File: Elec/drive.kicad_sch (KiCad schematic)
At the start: 37 parts, among them J1 PSU, J2 Conn_01x40, J3 Comm_Conn1, J4 Comm_Conn2, U1 DRV8434SPWPR, U2 DRV8434SPWPR

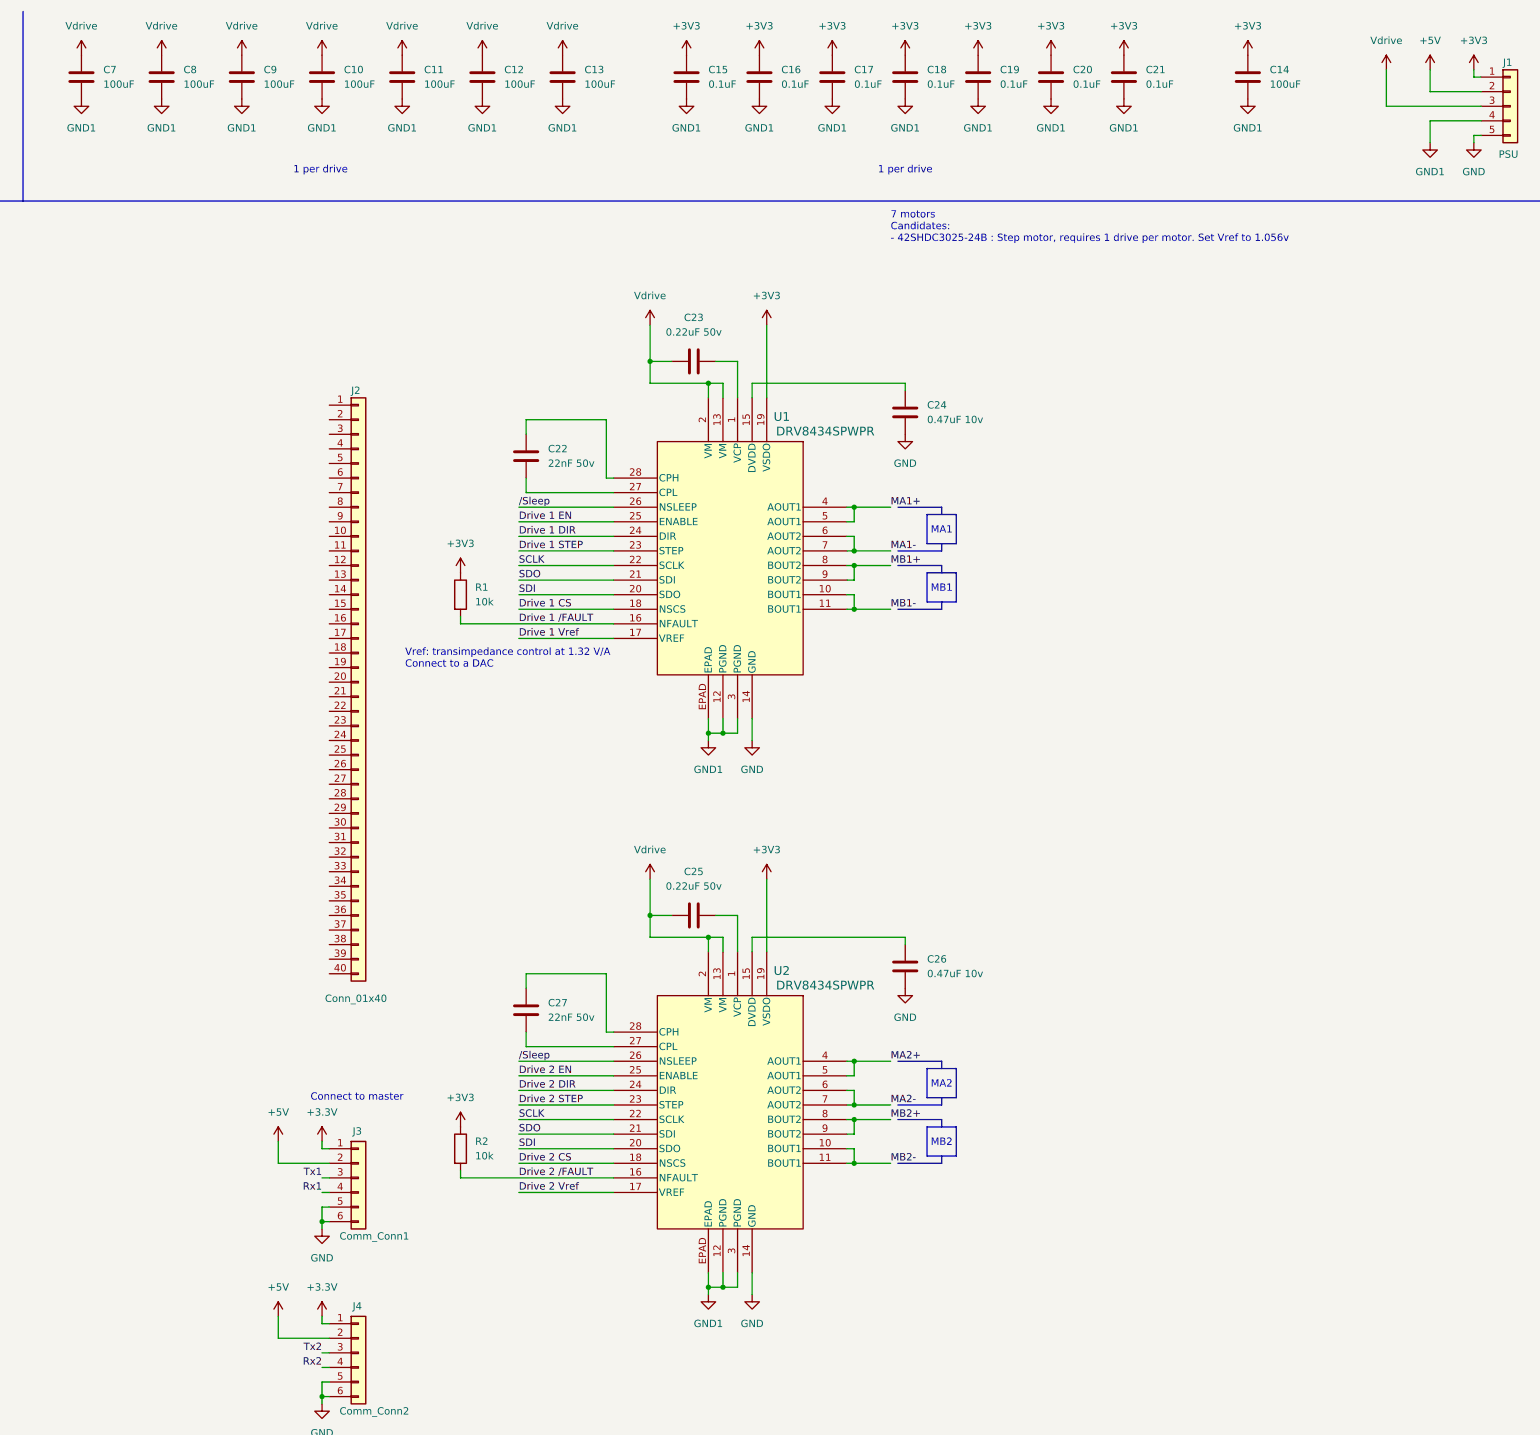
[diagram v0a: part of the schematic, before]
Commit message: Starting integration of the DRV8313PWPR drive
This drive supports BLDCs and BDCs.
Link: https://www.digikey.ca/en/products/detail/texas-instruments/DRV8313PWPR/3775439
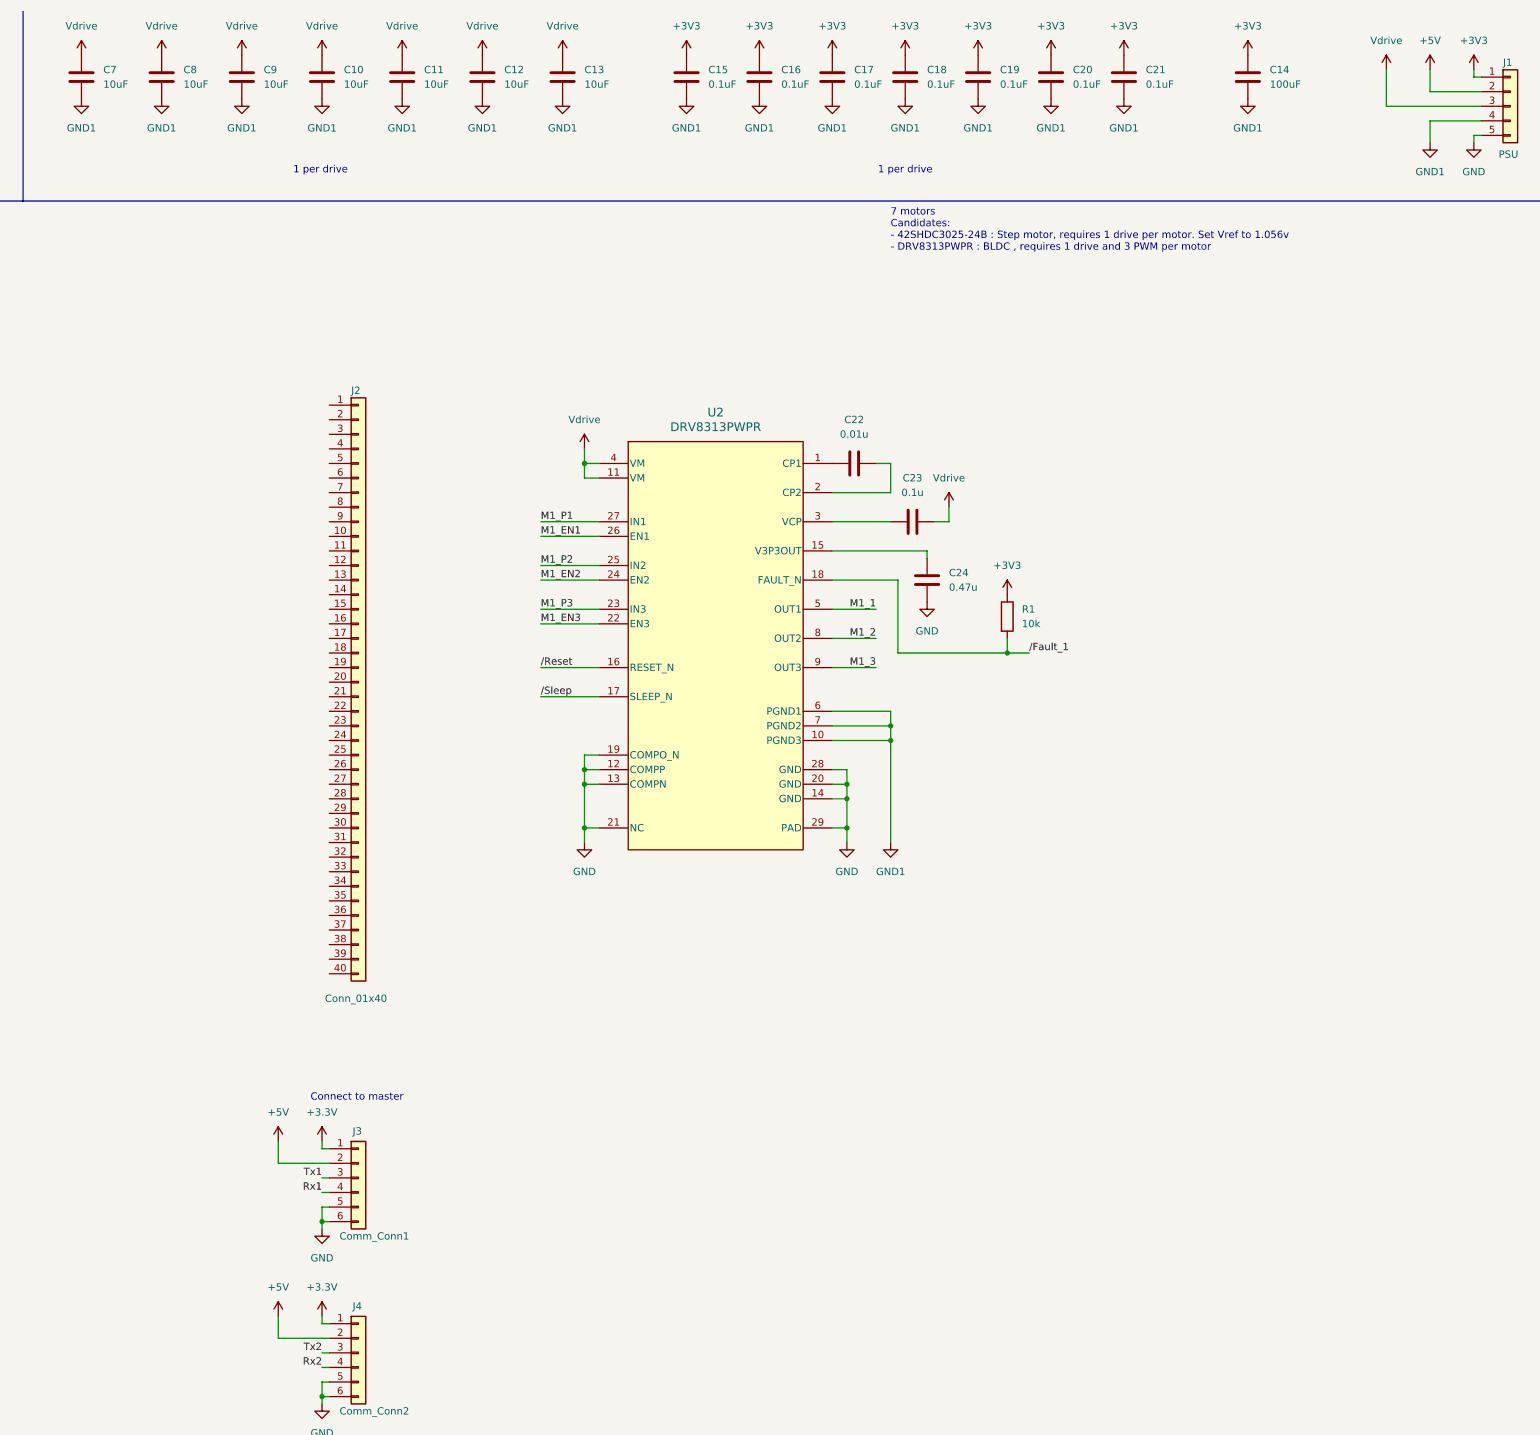
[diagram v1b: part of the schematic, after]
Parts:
- removed C25: 0.22uF 50v, symbol Device:C
- removed C26: 0.47uF 10v, symbol Device:C
- removed C27: 22nF 50v, symbol Device:C
- removed R2: 10k, symbol Device:R
- removed U1, U2: DRV8434SPWPR, PWP0028M_TEX, symbol DRV8434SPWPR:DRV8434SPWPR
- added U2: DRV8313PWPR, PWP0028F_N, symbol DRV8313PWPR:DRV8313PWPR
- C10, C11, C12, C13, C7, C8, C9: value 100uF -> 10uF
- C22: value 22nF 50v -> 0.01u
- C23: value 0.22uF 50v -> 0.1u
- C24: value 0.47uF 10v -> 0.47u
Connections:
- net GND: now also C24.1, U2.12 (COMPP), U2.13 (COMPN), U2.14 (GND), U2.19 (COMPO_N), U2.20 (GND), U2.21 (NC), U2.28 (GND), U2.29 (PAD); no longer C24.2
- net GND1: now also U2.10 (PGND3), U2.6 (PGND1), U2.7 (PGND2)
- net Vdrive: now also C23.2, U2.11 (VM), U2.4 (VM); no longer C23.1
- net /Sleep: now also U2.17 (SLEEP_N)
- net at C22.1: now also U2.1 (CP1)
- net at C22.2: now also U2.2 (CP2)
- net Drive 1 /FAULT renamed /Fault_1
- net /Fault_1: now also U2.18 (FAULT_N)
- new net: C24.2, U2.15 (V3P3OUT)
- new net: C23.1, U2.3 (VCP)
- new net M1_1: U2.5 (OUT1)
- new net M1_2: U2.8 (OUT2)
- new net M1_3: U2.9 (OUT3)
- new net M1_EN1: U2.26 (EN1)
- new net M1_EN2: U2.24 (EN2)
- new net M1_EN3: U2.22 (EN3)
- new net M1_P1: U2.27 (IN1)
- new net M1_P2: U2.25 (IN2)
- new net M1_P3: U2.23 (IN3)
- new net /Reset: U2.16 (RESET_N)
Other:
- note added: "7 motors Candidates: - 42SHDC3025-24B : Step motor, requires 1 drive per motor. Set Vref to 1.056v - DRV8313PWPR : BLDC , requires 1 drive and 3 PWM per motor"
- note removed: "7 motors Candidates: - 42SHDC3025-24B : Step motor, requires 1 drive per motor. Set Vref to 1.056v"
- note removed: "MA1"
- note removed: "MA2"
- note removed: "MB1"
- note removed: "MB2"
- note removed: "Vref: transimpedance control at 1.32 V/A Connect to a DAC"

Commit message: Introduced shift registers to control the drives PWMs
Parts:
- added C25, C28, C31, C34, C35, C36: 0.01u, symbol Device:C
- added C26, C29, C32, C37, C38, C39: 0.1u, symbol Device:C
- added C27, C30, C33, C40, C41, C42: 0.47u, symbol Device:C
- added C43, C44, C45, C46: 0.1uF, symbol Device:C
- added R2, R3, R4, R5, R6, R7: 10k, symbol Device:R
- added U10, U11, U12, U9: ~, symbol Custom:CD74HC4094DYYR
- added U3, U4, U5, U6, U7, U8: DRV8313PWPR, PWP0028F_N, symbol DRV8313PWPR:DRV8313PWPR
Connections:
- net +3V3: now also C43.1, C44.1, C45.1, C46.1, R2.1, R3.1, R4.1, R5.1, R6.1, R7.1, U10.16 (VCC), U11.16 (VCC), U12.16 (VCC), U9.16 (VCC)
- net GND: now also C27.1, C30.1, C33.1, C40.1, C41.1, C42.1, U10.8 (GND), U11.8 (GND), U12.8 (GND), U3.12 (COMPP), U3.13 (COMPN), U3.14 (GND), U3.19 (COMPO_N), U3.20 (GND), U3.21 (NC), U3.28 (GND), U3.29 (PAD), U4.12 (COMPP), U4.13 (COMPN), U4.14 (GND), U4.19 (COMPO_N), U4.20 (GND), U4.21 (NC), U4.28 (GND), U4.29 (PAD), U5.12 (COMPP), U5.13 (COMPN), U5.14 (GND), U5.19 (COMPO_N), U5.20 (GND), U5.21 (NC), U5.28 (GND), U5.29 (PAD), U6.12 (COMPP), U6.13 (COMPN), U6.14 (GND), U6.19 (COMPO_N), U6.20 (GND), U6.21 (NC), U6.28 (GND), U6.29 (PAD), U7.12 (COMPP), U7.13 (COMPN), U7.14 (GND), U7.19 (COMPO_N), U7.20 (GND), U7.21 (NC), U7.28 (GND), U7.29 (PAD), U8.12 (COMPP), U8.13 (COMPN), U8.14 (GND), U8.19 (COMPO_N), U8.20 (GND), U8.21 (NC), U8.28 (GND), U8.29 (PAD), U9.8 (GND)
- net GND1: now also C43.2, C44.2, C45.2, C46.2, U3.10 (PGND3), U3.6 (PGND1), U3.7 (PGND2), U4.10 (PGND3), U4.6 (PGND1), U4.7 (PGND2), U5.10 (PGND3), U5.6 (PGND1), U5.7 (PGND2), U6.10 (PGND3), U6.6 (PGND1), U6.7 (PGND2), U7.10 (PGND3), U7.6 (PGND1), U7.7 (PGND2), U8.10 (PGND3), U8.6 (PGND1), U8.7 (PGND2)
- net M1_P1: now also U9.4 (Q0)
- net M1_P2: now also U9.5 (Q1)
- net M1_P3: now also U9.6 (Q2)
- net Vdrive: now also C26.2, C29.2, C32.2, C37.2, C38.2, C39.2, U3.11 (VM), U3.4 (VM), U4.11 (VM), U4.4 (VM), U5.11 (VM), U5.4 (VM), U6.11 (VM), U6.4 (VM), U7.11 (VM), U7.4 (VM), U8.11 (VM), U8.4 (VM)
- net /Fault_1: now also R2.2, R3.2, R4.2, R5.2, R6.2, R7.2, U3.18 (FAULT_N), U4.18 (FAULT_N), U5.18 (FAULT_N), U6.18 (FAULT_N), U7.18 (FAULT_N), U8.18 (FAULT_N)
- net /Reset: now also U3.16 (RESET_N), U4.16 (RESET_N), U5.16 (RESET_N), U6.16 (RESET_N), U7.16 (RESET_N), U8.16 (RESET_N)
- net /Sleep: now also U10.15 (OE), U11.15 (OE), U12.15 (OE), U3.17 (SLEEP_N), U4.17 (SLEEP_N), U5.17 (SLEEP_N), U6.17 (SLEEP_N), U7.17 (SLEEP_N), U8.17 (SLEEP_N), U9.15 (OE)
- new net: C39.1, U8.3 (VCP)
- new net: C28.1, U4.1 (CP1)
- new net: C28.2, U4.2 (CP2)
- new net: C34.1, U6.1 (CP1)
- new net: C40.2, U6.15 (V3P3OUT)
- new net: C34.2, U6.2 (CP2)
- new net: C37.1, U6.3 (VCP)
- new net: C36.1, U8.1 (CP1)
- new net: C36.2, U8.2 (CP2)
- new net: C30.2, U4.15 (V3P3OUT)
- new net: C29.1, U4.3 (VCP)
- new net: C38.1, U7.3 (VCP)
- new net: C35.1, U7.1 (CP1)
- new net: C35.2, U7.2 (CP2)
- new net: C26.1, U3.3 (VCP)
- new net: C32.1, U5.3 (VCP)
- new net: C31.1, U5.1 (CP1)
- new net: C31.2, U5.2 (CP2)
- new net: C33.2, U5.15 (V3P3OUT)
- new net: C42.2, U8.15 (V3P3OUT)
- new net: C25.1, U3.1 (CP1)
- new net: C25.2, U3.2 (CP2)
- new net: C27.2, U3.15 (V3P3OUT)
- new net: C41.2, U7.15 (V3P3OUT)
- new net DATA_M1-2: U9.2 (DATA)
- new net DATA_M3-4: U10.2 (DATA)
- new net DATA_M5-6: U11.2 (DATA)
- new net DATA_M7: U12.2 (DATA)
- new net M2_1: U3.5 (OUT1)
- new net M2_2: U3.8 (OUT2)
- new net M2_3: U3.9 (OUT3)
- new net M2_EN1: U3.26 (EN1)
- new net M2_EN2: U3.24 (EN2)
- new net M2_EN3: U3.22 (EN3)
- new net M2_P1: U3.27 (IN1), U9.7 (Q3)
- new net M2_P2: U3.25 (IN2), U9.14 (Q4)
- new net M2_P3: U3.23 (IN3), U9.13 (Q5)
- new net M3_1: U4.5 (OUT1)
- new net M3_2: U4.8 (OUT2)
- new net M3_3: U4.9 (OUT3)
- new net M3_EN1: U4.26 (EN1)
- new net M3_EN2: U4.24 (EN2)
- new net M3_EN3: U4.22 (EN3)
- new net M3_P1: U10.4 (Q0), U4.27 (IN1)
- new net M3_P2: U10.5 (Q1), U4.25 (IN2)
- new net M3_P3: U10.6 (Q2), U4.23 (IN3)
- new net M4_1: U5.5 (OUT1)
- new net M4_2: U5.8 (OUT2)
- new net M4_3: U5.9 (OUT3)
- new net M4_EN1: U5.26 (EN1)
- new net M4_EN2: U5.24 (EN2)
- new net M4_EN3: U5.22 (EN3)
- new net M4_P1: U10.7 (Q3), U5.27 (IN1)
- new net M4_P2: U10.14 (Q4), U5.25 (IN2)
- new net M4_P3: U10.13 (Q5), U5.23 (IN3)
- new net M5_1: U6.5 (OUT1)
- new net M5_2: U6.8 (OUT2)
- new net M5_3: U6.9 (OUT3)
- new net M5_EN1: U6.26 (EN1)
- new net M5_EN2: U6.24 (EN2)
- new net M5_EN3: U6.22 (EN3)
- new net M5_P1: U11.4 (Q0), U6.27 (IN1)
- new net M5_P2: U11.5 (Q1), U6.25 (IN2)
- new net M5_P3: U11.6 (Q2), U6.23 (IN3)
- new net M6_1: U7.5 (OUT1)
- new net M6_2: U7.8 (OUT2)
- new net M6_3: U7.9 (OUT3)
- new net M6_EN1: U7.26 (EN1)
- new net M6_EN2: U7.24 (EN2)
- new net M6_EN3: U7.22 (EN3)
- new net M6_P1: U11.7 (Q3), U7.27 (IN1)
- new net M6_P2: U11.14 (Q4), U7.25 (IN2)
- new net M6_P3: U11.13 (Q5), U7.23 (IN3)
- new net M7_1: U8.5 (OUT1)
- new net M7_2: U8.8 (OUT2)
- new net M7_3: U8.9 (OUT3)
- new net M7_EN1: U8.26 (EN1)
- new net M7_EN2: U8.24 (EN2)
- new net M7_EN3: U8.22 (EN3)
- new net M7_P1: U12.4 (Q0), U8.27 (IN1)
- new net M7_P2: U12.5 (Q1), U8.25 (IN2)
- new net M7_P3: U12.6 (Q2), U8.23 (IN3)
- new net SEQ_Update_M1-2: U9.1 (STR)
- new net SEQ_Update_M3-4: U10.1 (STR)
- new net SEQ_Update_M5-6: U11.1 (STR)
- new net SEQ_Update_M7: U12.1 (STR)
- new net Serial_CLK: U10.3 (CP), U11.3 (CP), U12.3 (CP), U9.3 (CP)
- no-connect marks 0 -> 19
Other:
- note added: "1 per shift register"
- note added: "12 PWM channels"
- moved on the sheet: C22, C23, C24, J1, J2, J3, J4, R1, U1, U2
